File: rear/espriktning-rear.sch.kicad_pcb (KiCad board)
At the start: 2 copper layers, 20 x 75 mm, 28 parts, among them J1 USB_C_Receptacle_USB2.0, J4 Conn_01x08, SW1 Reset, SW2 Flash

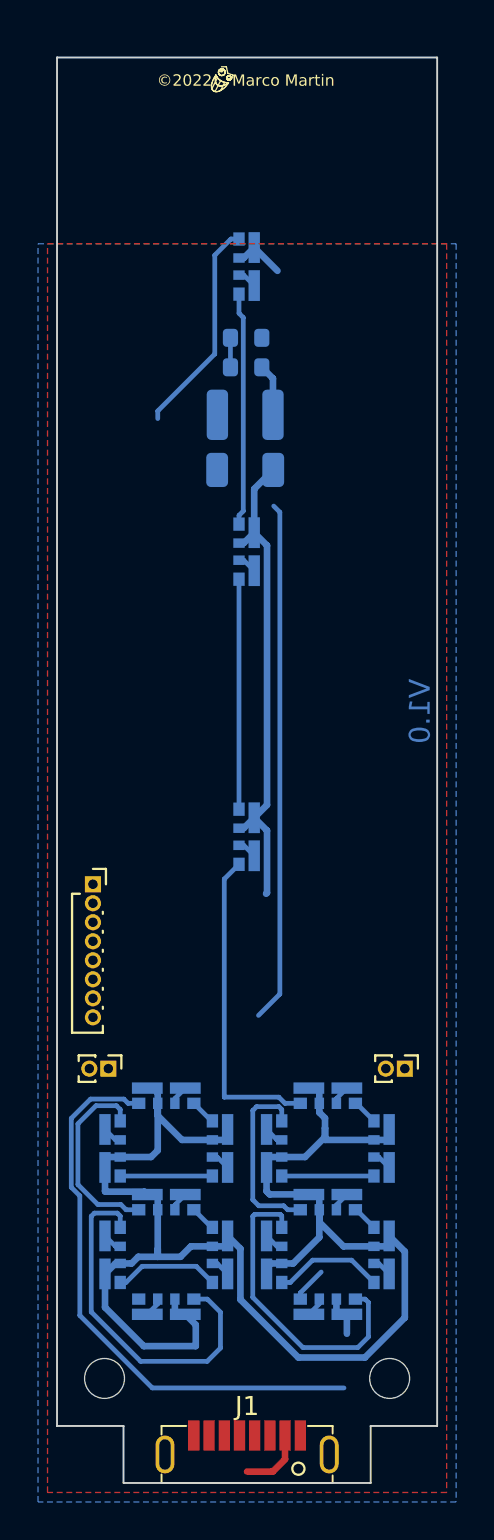
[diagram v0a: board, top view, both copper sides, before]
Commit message: relayout to actually fit
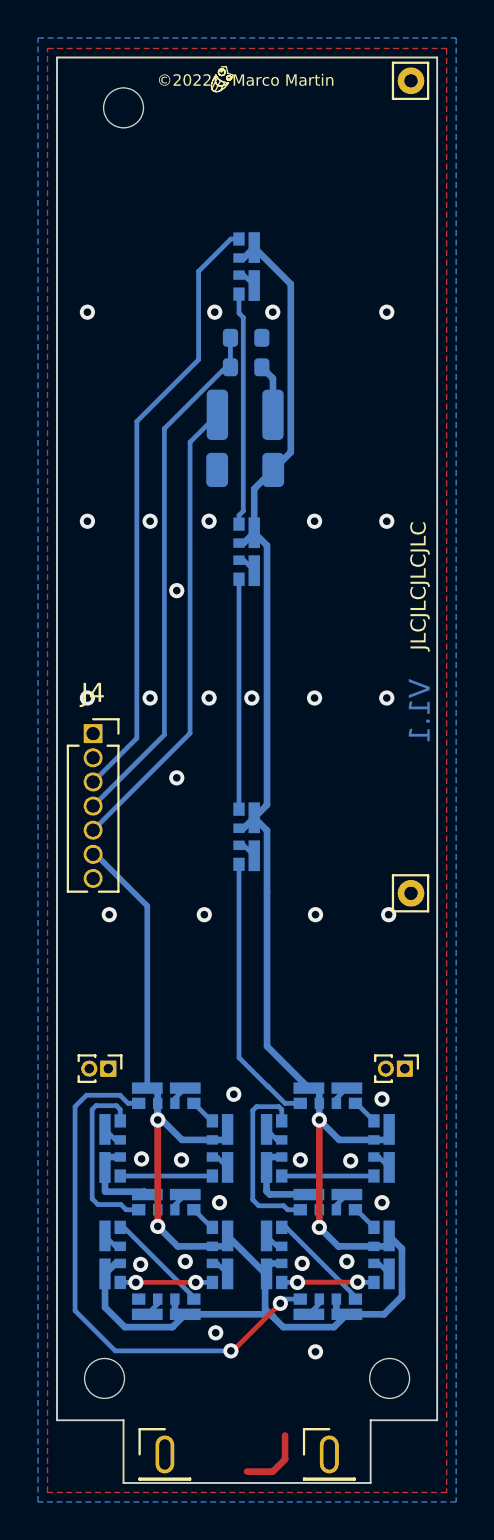
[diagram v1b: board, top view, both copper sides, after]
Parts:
- removed J1: USB_C_Receptacle_USB2.0, espriktning:usb-c-vertical-8
- added J2: Conn_01x01_Male, Connector_Pin:Pin_D0.7mm_L6.5mm_W1.8mm_FlatFork, F.Cu at (48.6, 74.0)
- added J3: Conn_01x01_Male, Connector_Pin:Pin_D0.7mm_L6.5mm_W1.8mm_FlatFork, F.Cu at (48.6, 31.2)
- added REF**: MountingHole_2.1mm, MountingHole:MountingHole_2.1mm, F.Cu at (33.5, 32.6)
- added REF**: PinHeader_1x01_P2.54mm_Vertical, Connector_PinHeader_2.54mm:PinHeader_1x01_P2.54mm_Vertical, F.Cu at (44.3, 103.5)
- added REF**: PinHeader_1x01_P2.54mm_Vertical, Connector_PinHeader_2.54mm:PinHeader_1x01_P2.54mm_Vertical, F.Cu at (35.7, 103.5)
- J4: footprint Connector_PinSocket_1.00mm:PinSocket_1x08_P1.00mm_Vertical -> Connector_PinSocket_1.27mm:PinSocket_1x07_P1.27mm_Vertical
- moved J4 7.93 mm to (31.9, 65.6)
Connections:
- C10 pad 1: Net-(D4-Pad4) -> +5V
- J4 pad 1: +3V3 -> TX
- J4 pad 2: TX -> RX
- J4 pad 3: RX -> GPIO14
- J4 pad 5: GPIO9 -> +3V3
- J4 pad 6: GPIO10 -> +5V
- J4 pad 7: +5V -> GND
- SW1 pad 1: RST -> unconnected-(SW1-Pad1)
- SW2 pad 1: GPIO0 -> unconnected-(SW2-Pad1)
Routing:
- net +5V: track 114.9 -> 145.5 mm, vias 0 -> 4
- net GPIO10: track 27.4 -> 0.00 mm
- net ADC: track 1.55 -> 27.8 mm
- net +3V3: track 0.00 -> 24.6 mm
- net GPIO14: track 11.5 -> 32.0 mm
- net Net-(D17-Pad4): track 19.0 -> 5.49 mm
- net Net-(D10-Pad4): track 16.5 -> 5.51 mm
- net Net-(D11-Pad4): track 32.0 -> 28.4 mm, vias 0 -> 2
- net Net-(D19-Pad2): track 3.52 -> 0.00 mm
- net (no net): track 0.00 -> 3.52 mm
- net Net-(D4-Pad4): track 16.7 -> 14.4 mm
- net Net-(D10-Pad2): track 5.82 -> 4.86 mm, vias 0 -> 2
- net Net-(D16-Pad4): track 5.55 -> 4.85 mm, vias 0 -> 2
- net Net-(D14-Pad4): track 10.3 -> 9.63 mm
- net GND: vias 0 -> 35
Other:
- outline, holes or cut-outs redrawn
- board text added: "V1.1"
- board text removed: "V1.0"
